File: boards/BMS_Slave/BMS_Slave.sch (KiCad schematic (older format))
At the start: 63 parts, among them J1 Mounting_Hole_4-40, J2 Mounting_Hole_4-40, J3 Mounting_Hole_4-40, J4 Mounting_Hole_4-40, J5 MicroFit_12, J6 MicroFit_20, J7 NanoFit_2, J8 NanoFit_2, Q1 Q_NPN_BCE, T1 T_LAN_7490100111A, U1 LTC6811-1, U2 24AA01, U3 MCP6001, U4 LTC1380, U5 LTC1380, U6 MCP6001

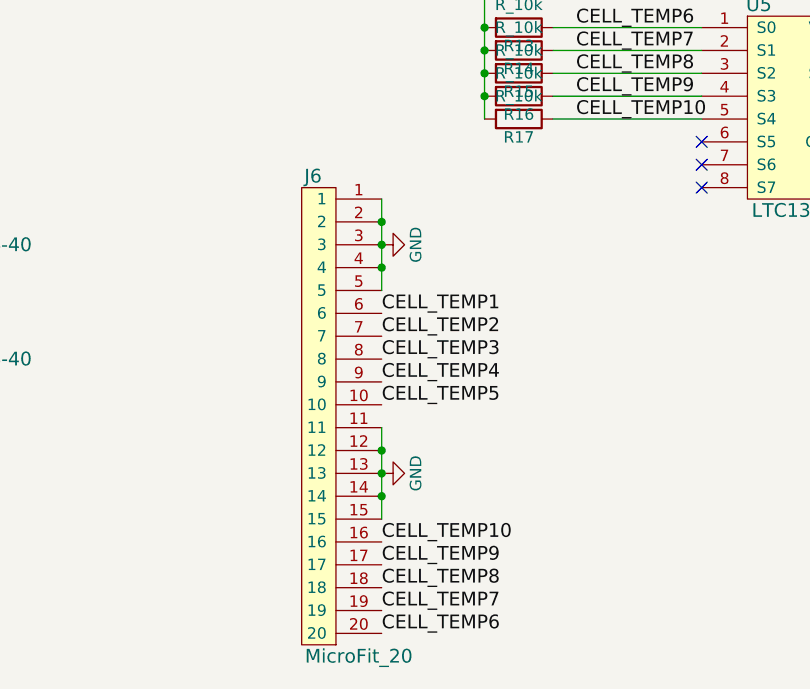
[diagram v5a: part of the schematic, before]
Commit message: BMS_Slave: updated tracing/connector for temp sense
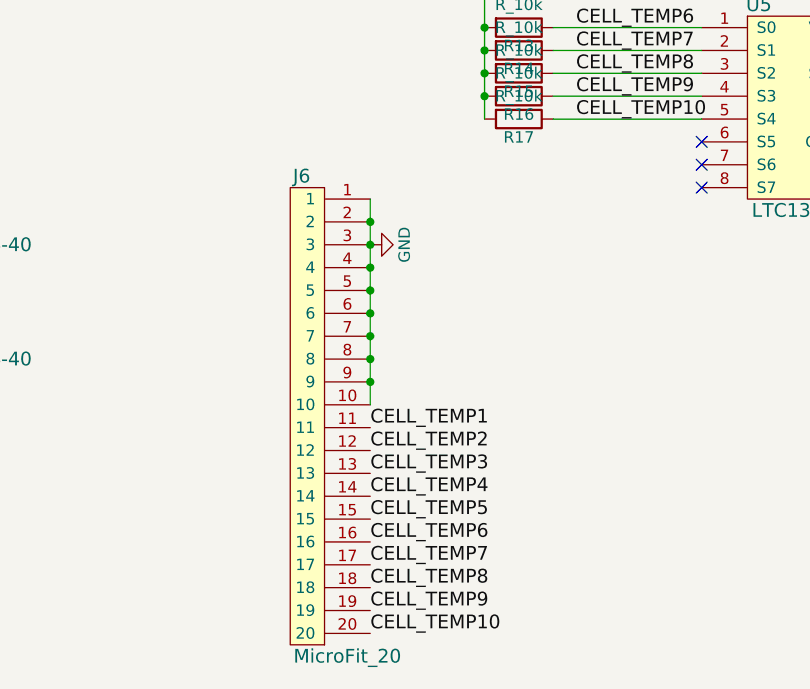
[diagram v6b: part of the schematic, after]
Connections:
- net CELL_TEMP1: now also J6.11; no longer J6.6
- net CELL_TEMP10: now also J6.20; no longer J6.16
- net CELL_TEMP2: now also J6.12; no longer J6.7
- net CELL_TEMP3: now also J6.13; no longer J6.8
- net CELL_TEMP4: now also J6.14; no longer J6.9
- net CELL_TEMP5: now also J6.15; no longer J6.10
- net CELL_TEMP6: now also J6.16; no longer J6.20
- net CELL_TEMP7: now also J6.17; no longer J6.19
- net CELL_TEMP9: now also J6.19; no longer J6.17
- net GND: now also J6.10, J6.6, J6.7, J6.8, J6.9; no longer J6.11, J6.12, J6.13, J6.14, J6.15
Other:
- moved on the sheet: J6
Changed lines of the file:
@@
 	1    0    0    -1
 $EndComp
-Text Label 6400 8850 0    60   ~ 0
+Text Label 6350 9350 0    60   ~ 0
 CELL_TEMP1
-Text Label 6400 8950 0    60   ~ 0
+Text Label 6350 9450 0    60   ~ 0
 CELL_TEMP2
-Text Label 6400 9050 0    60   ~ 0
+Text Label 6350 9550 0    60   ~ 0
 CELL_TEMP3
-Text Label 6400 9150 0    60   ~ 0
+Text Label 6350 9650 0    60   ~ 0
 CELL_TEMP4
-Text Label 6400 9250 0    60   ~ 0
+Text Label 6350 9750 0    60   ~ 0
 CELL_TEMP5
-Text Label 6400 10250 0    60   ~ 0
+Text Label 6350 9850 0    60   ~ 0
 CELL_TEMP6
-Text Label 6400 10150 0    60   ~ 0
+Text Label 6350 9950 0    60   ~ 0
 CELL_TEMP7
-Text Label 6400 10050 0    60   ~ 0
+Text Label 6350 10050 0    60   ~ 0
 CELL_TEMP8
-Text Label 6400 9950 0    60   ~ 0
+Text Label 6350 10150 0    60   ~ 0
 CELL_TEMP9
-Text Label 6400 9850 0    60   ~ 0
+Text Label 6350 10250 0    60   ~ 0
 CELL_TEMP10
 NoConn ~ 9200 950
@@
 NoConn ~ 800  4150
 $Comp
-L GND #PWR017
-U 1 1 5A00BA8F
-P 6400 9550
-F 0 "#PWR017" H 6400 9300 50  0001 C CNN
-F 1 "GND" H 6400 9400 50  0000 C CNN
-F 2 "" H 6400 9550 50  0001 C CNN
-F 3 "" H 6400 9550 50  0001 C CNN
-	1    6400 9550
-	0    -1   -1   0
-$EndComp
-$Comp
 L GND #PWR018
 U 1 1 5A59223B
-P 6400 8550
-F 0 "#PWR018" H 6400 8300 50  0001 C CNN
-F 1 "GND" H 6400 8400 50  0000 C CNN
-F 2 "" H 6400 8550 50  0001 C CNN
-F 3 "" H 6400 8550 50  0001 C CNN
-	1    6400 8550
+P 6350 8550
+F 0 "#PWR018" H 6350 8300 50  0001 C CNN
+F 1 "GND" H 6350 8400 50  0000 C CNN
+F 2 "" H 6350 8550 50  0001 C CNN
+F 3 "" H 6350 8550 50  0001 C CNN
+	1    6350 8550
 	0    -1   -1   0
 $EndComp
@@
 L MicroFit_20 J6
 U 1 1 5A0F4926
-P 5800 8100
-F 0 "J6" H 6100 7950 60  0000 C CNN
-F 1 "MicroFit_20" H 6300 5850 60  0000 C CNN
-F 2 "footprints:Molex_Microfit3_Header_02x10_Angled_OEM" H 5800 8100 60  0001 C CNN
-F 3 "" H 5800 8100 60  0001 C CNN
-	1    5800 8100
+P 5750 8100
+F 0 "J6" H 6050 7950 60  0000 C CNN
+F 1 "MicroFit_20" H 6250 5850 60  0000 C CNN
+F 2 "footprints:Molex_Microfit3_Header_02x10_Angled_OEM" H 5750 8100 60  0001 C CNN
+F 3 "" H 5750 8100 60  0001 C CNN
+	1    5750 8100
 	1    0    0    -1
 $EndComp
@@
 	1800 750  4750 750
 Wire Wire Line
-	6400 8350 6400 8750
-Connection ~ 6400 8450
-Connection ~ 6400 8550
-Connection ~ 6400 8650
-Wire Wire Line
-	6400 9350 6400 9750
-Connection ~ 6400 9450
-Connection ~ 6400 9550
-Connection ~ 6400 9650
+	6350 8350 6350 9250
+Connection ~ 6350 8450
+Connection ~ 6350 8550
+Connection ~ 6350 8650
+Connection ~ 6350 8750
+Connection ~ 6350 8850
+Connection ~ 6350 8950
+Connection ~ 6350 9050
+Connection ~ 6350 9150
 $EndSCHEMATC

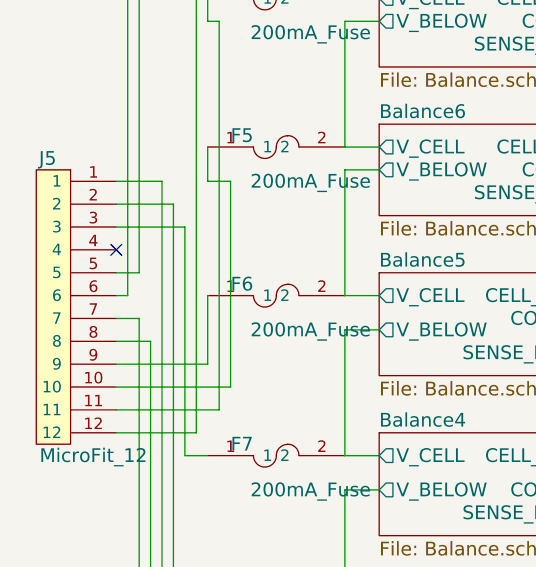
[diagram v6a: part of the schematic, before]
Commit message: BMS Slave: tied pin 4 to pin 7
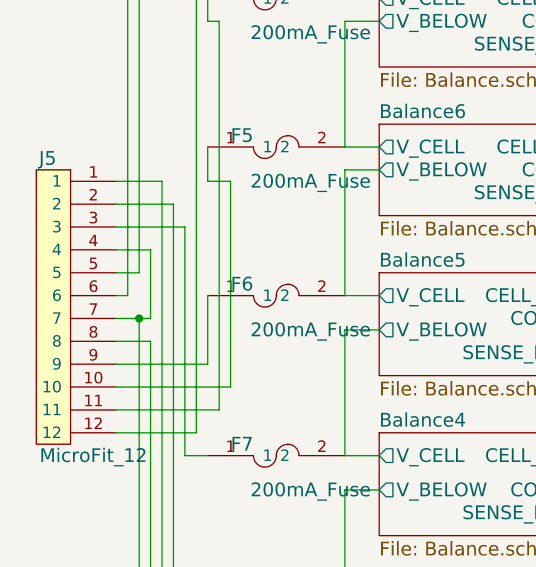
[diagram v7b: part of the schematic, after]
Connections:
- net at F11.1, J5.7: now also J5.4
- no-connect marks 17 -> 16
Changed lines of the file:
@@
 	1    0    0    -1
 $EndComp
-NoConn ~ 800  4150
 $Comp
 L GND #PWR018
@@
 	950  6950 950  4550
 Wire Wire Line
-	900  4450 800  4450
+	800  4450 950  4450
 Wire Wire Line
 	900  4450 900  7500
@@
 Connection ~ 6350 9050
 Connection ~ 6350 9150
+Wire Wire Line
+	800  4150 950  4150
+Wire Wire Line
+	950  4150 950  4450
+Connection ~ 900  4450
 $EndSCHEMATC

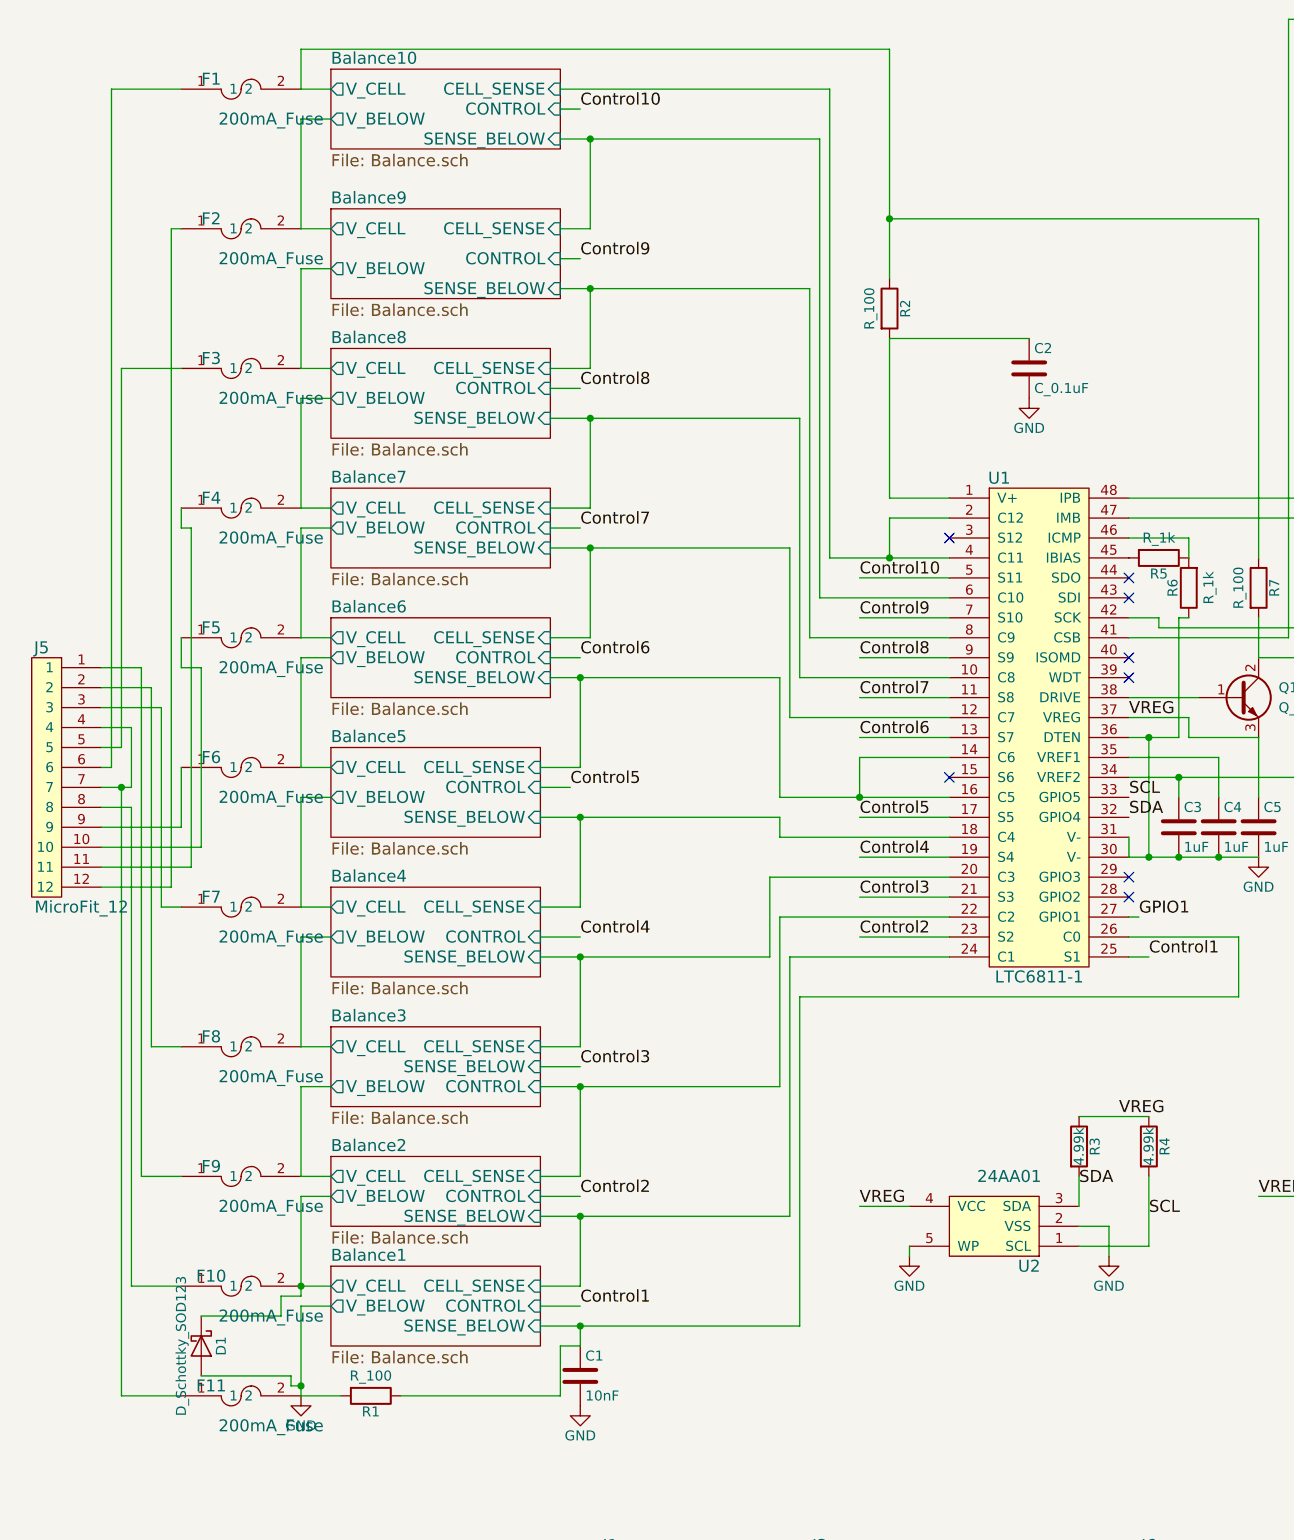
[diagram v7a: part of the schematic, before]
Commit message: BMS Slave: corrected mosfet routing
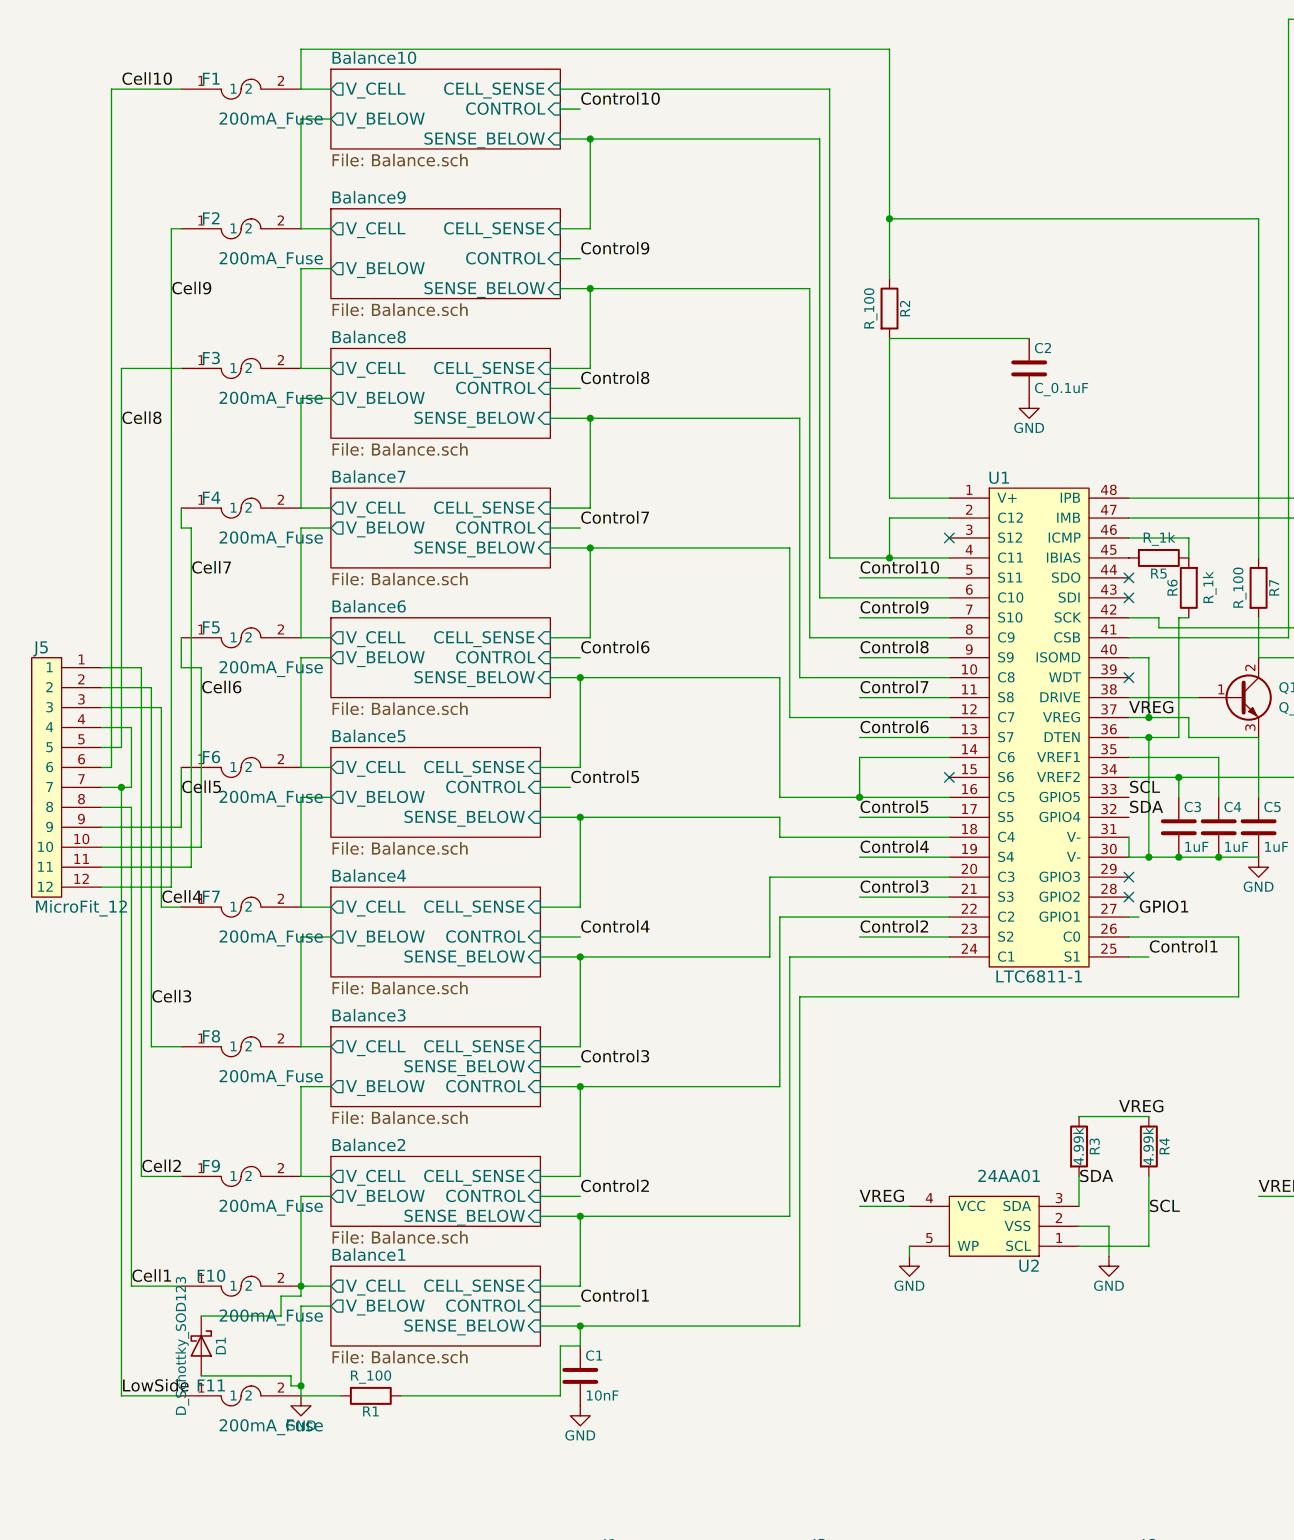
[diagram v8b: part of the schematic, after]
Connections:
- net VREG: now also U1.40 (ISOMD)
- net Cell10: now reaches F1.1, J5.6
- net Cell9: now reaches F2.1, J5.12
- net Cell8: now reaches F3.1, J5.5
- net Cell7: now reaches F4.1, J5.11
- net Cell6: now reaches F5.1, J5.10
- net Cell5: now reaches F6.1, J5.9
- net Cell4: now reaches F7.1, J5.3
- net Cell3: now reaches F8.1, J5.2
- net Cell2: now reaches F9.1, J5.1
- net Cell1: now reaches F10.1, J5.8
- net LowSide: now reaches F11.1, J5.4, J5.7
- no-connect marks 16 -> 15
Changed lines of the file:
@@
 NoConn ~ 7800 8300
 NoConn ~ 5950 3900
-NoConn ~ 5950 3800
 NoConn ~ 5950 3500
 NoConn ~ 5950 3400
@@
 	950  4150 950  4450
 Connection ~ 900  4450
+Wire Wire Line
+	5950 3800 6050 3800
+Wire Wire Line
+	6050 3800 6050 4100
+Connection ~ 6050 4100
+Text Label 900  950  0    60   ~ 0
+Cell10
+Text Label 1150 2000 0    60   ~ 0
+Cell9
+Text Label 900  2650 0    60   ~ 0
+Cell8
+Text Label 1250 3400 0    60   ~ 0
+Cell7
+Text Label 1300 4000 0    60   ~ 0
+Cell6
+Text Label 1200 4500 0    60   ~ 0
+Cell5
+Text Label 1100 5050 0    60   ~ 0
+Cell4
+Text Label 1050 5550 0    60   ~ 0
+Cell3
+Text Label 1000 6400 0    60   ~ 0
+Cell2
+Text Label 950  6950 0    60   ~ 0
+Cell1
+Text Label 900  7500 0    60   ~ 0
+LowSide
 $EndSCHEMATC
